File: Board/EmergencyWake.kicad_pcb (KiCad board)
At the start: 2 copper layers, 100 x 67 mm, 147 parts, among them J1 USB_C_Receptacle_USB2.0, J10 Conn_01x04, J2 Micro_SD_Card_Det, J3 Conn_01x03, J4 Conn_01x02, J5 Conn_01x05, J6 Conn_01x04, J7 Conn_01x02, J8 Conn_01x04, J9 Conn_01x04, Q1 AO3400A, Q2 AO3401A, Q3 AO3400A, SW1 SW_DPDT_x2, SW2 SW_Push, SW3 SW_Push, SW4 SW_Push, U1 M24C02-WMN, U10 L9110S, U11 SRV05-4, U2 AMS1117-3.3, U3 MC34063AD, U4 STM32F407VETx, U5 LM4670, U6 173950378, U7 PT6312B, U8 EL357N-G, U9 EL357N-G, Y1 32,768

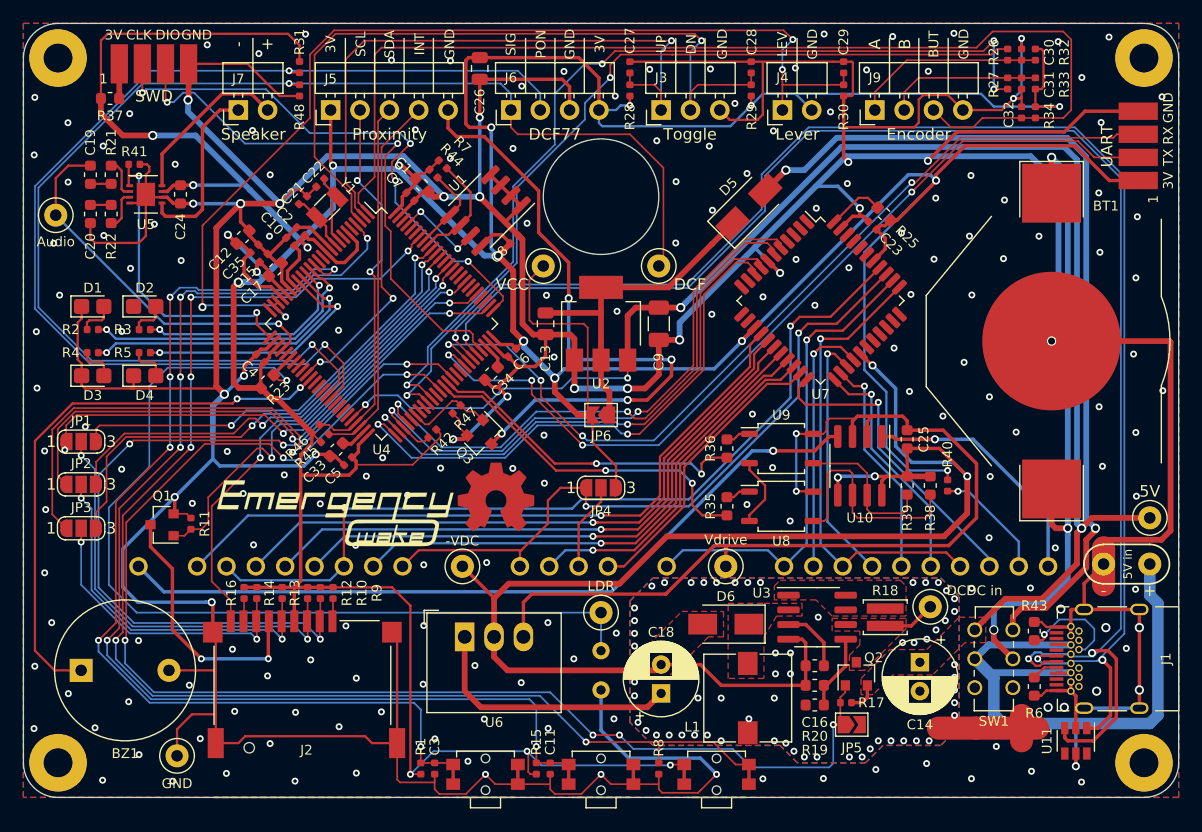
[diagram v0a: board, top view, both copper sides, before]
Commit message: [Board] Added OR gate for wakeup signal
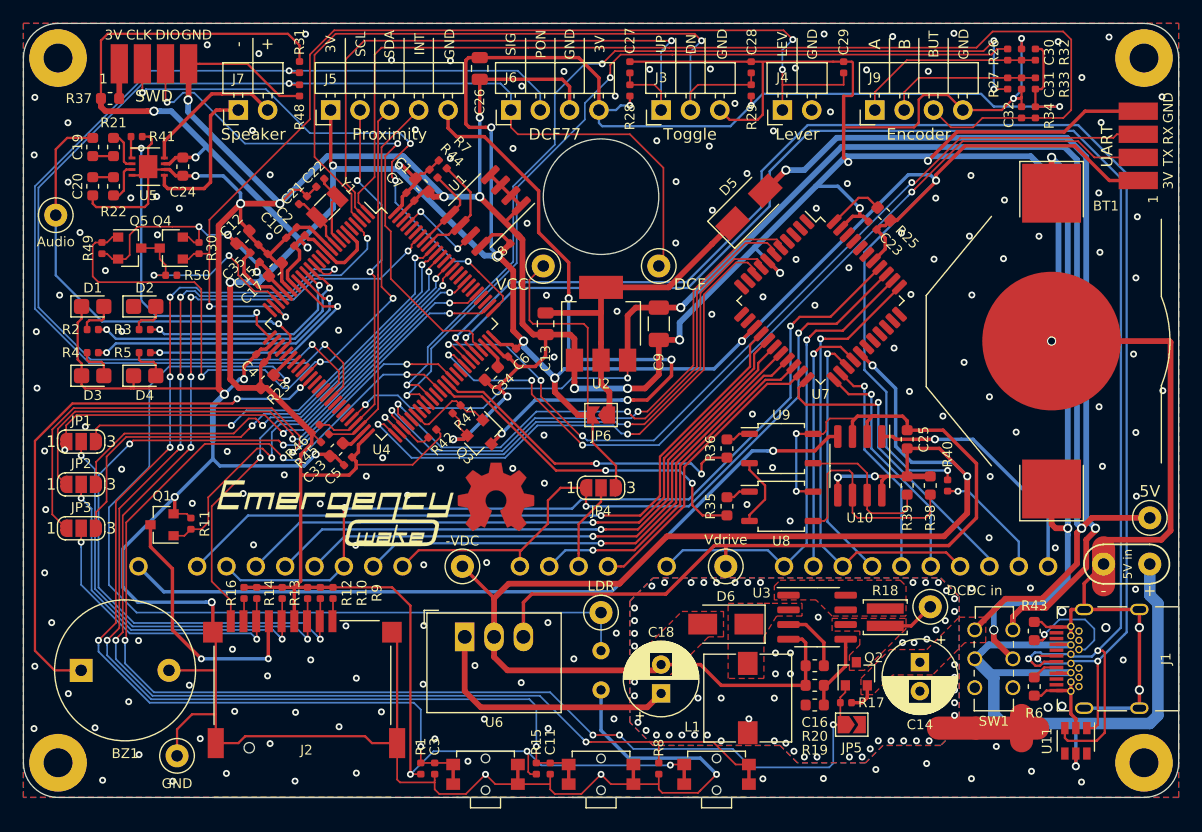
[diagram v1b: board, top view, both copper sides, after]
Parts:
- added Q4: AO3401A, Package_TO_SOT_SMD:SOT-23, F.Cu at (112.8, 119.5)
- added Q5: AO3401A, Package_TO_SOT_SMD:SOT-23, F.Cu at (109.2, 119.5)
- added R49: 100k, Resistor_SMD:R_0402_1005Metric, F.Cu at (106.8, 119.4)
- added R50: 100k, Resistor_SMD:R_0402_1005Metric, F.Cu at (112.8, 121.8)
- moved R30 57.4 mm to (115.2, 119.4), turned to 90 degrees
- moved C20 2.41 mm to (106.0, 114.1)
- moved R22 2.41 mm to (107.8, 114.1)
- moved R41 2.41 mm to (109.8, 109.8)
- moved U5 2.41 mm to (110.8, 112.4)
- moved C19 2.41 mm to (106.0, 110.7)
- moved C24 2.41 mm to (113.8, 112.4)
- moved R21 2.41 mm to (107.8, 110.7)
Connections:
- J4 pad 2: VCC -> GND
- R30 pad 2: GND -> VCC
- U4 pad 23: /LEVER -> /WAKEUP
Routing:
- net /I2C_INT: track 28.3 -> 63.0 mm, vias 2 -> 3
- net /WAKEUP: track 0.00 -> 18.8 mm, vias 0 -> 2
- net VCC: track 501.3 -> 512.9 mm, vias 21 -> 22
- net /AUDIO_OUT: track 32.8 -> 38.5 mm
- net /AUDIO_EN: track 26.5 -> 29.2 mm
- net /USB_DP: track 135.1 -> 132.8 mm
- net /SP+: track 15.5 -> 13.6 mm
- net /SP-: track 14.6 -> 12.7 mm
- net /USB_DM: track 129.9 -> 128.7 mm
- net /LEVER: track 91.1 -> 92.1 mm
- net GND: track 614.4 -> 614.5 mm, vias 202 -> 199

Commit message: [Board] New fabrication files
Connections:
- TP4 pad 1: VCC -> Net-(C13-Pad1)
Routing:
- net VCC: track 512.9 -> 495.1 mm
- net Net-(C13-Pad1): track 29.9 -> 34.0 mm
- net GND: vias 199 -> 209

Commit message: [Board] Some minor changes
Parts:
- removed the G*** at (149.0, 132.0)
- added C36: 22u,25V, Capacitor_SMD:C_0805_2012Metric, F.Cu at (123.0, 144.7)
- added G***: LOGO, Logo:EmergencyWake_Logo_20mm, B.Cu at (166.9, 154.0)
- C21, C22: value 6p -> 15p
- C26: value 10u,50V -> 10u,25V
- C9: value 10u,50V -> 10u,25V; footprint Capacitor_SMD:C_1206_3216Metric -> Capacitor_SMD:C_0805_2012Metric
- moved R11 0.10 mm to (114.5, 143.4)
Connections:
- C24 pad 1: VCC -> +5V
- U5 pad 7: VCC -> +5V
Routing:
- net +5V: track 132.6 -> 196.5 mm, vias 4 -> 7
- net GND: track 614.5 -> 577.2 mm, vias 209 -> 213
- net VCC: track 495.1 -> 490.3 mm, vias 22 -> 21
- net /SD_EN: track 37.3 -> 41.6 mm
- net /SD_DET: track 41.3 -> 39.9 mm
- net /SD_MOSI: track 38.4 -> 39.2 mm
- net Net-(DISP1-Pad32): track 67.0 -> 67.7 mm
- net /SWCLK: track 47.9 -> 48.6 mm
- net /SWDIO: track 48.6 -> 49.3 mm
- net Net-(J5-Pad5): track 55.2 -> 55.8 mm
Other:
- board text added: "BOOT0"
- board text added: "JH 2020"
- board text added: "Reset"
- board text added: "User"

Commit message: [Board] Final changes for order
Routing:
- net GND: track 577.2 -> 578.0 mm
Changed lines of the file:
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@@
   )
   (setup
-    (last_trace_width 0.5)
+    (last_trace_width 0.15)
     (user_trace_width 0.15)
     (user_trace_width 0.2)
@@
   (segment (start 187.2 111.5) (end 178.7 111.5) (width 0.5) (layer B.Cu) (net 4))
   (segment (start 178.7 111.5) (end 171.2 111.5) (width 0.5) (layer B.Cu) (net 4))
-  (segment (start 178.7 111.5) (end 178.686812 111.5) (width 0.3) (layer B.Cu) (net 4))
-  (segment (start 178.643405 111.543407) (end 178.293406 111.893406) (width 0.3) (layer B.Cu) (net 4))
-  (via (at 178.293406 111.893406) (size 0.7) (drill 0.4) (layers F.Cu B.Cu) (net 4))
-  (segment (start 178.686812 111.5) (end 178.643405 111.543407) (width 0.3) (layer B.Cu) (net 4))
   (segment (start 168.6 114.1) (end 170.5 114.1) (width 0.3) (layer B.Cu) (net 4))
   (segment (start 171.2 111.5) (end 168.6 114.1) (width 0.5) (layer B.Cu) (net 4))
@@
   (segment (start 142.842947 118.357053) (end 139.5 115.014106) (width 0.5) (layer F.Cu) (net 4))
   (via (at 139.5 115.000016) (size 0.8) (drill 0.5) (layers F.Cu B.Cu) (net 4))
-  (segment (start 178.3 111.9) (end 178.293406 111.893406) (width 0.3) (layer F.Cu) (net 4))
-  (segment (start 196.5 107.6) (end 191.9 107.6) (width 0.3) (layer F.Cu) (net 4))
-  (segment (start 180.8 109.4) (end 178.3 111.9) (width 0.3) (layer F.Cu) (net 4))
-  (segment (start 191.9 107.6) (end 190.1 109.4) (width 0.3) (layer F.Cu) (net 4))
-  (segment (start 190.1 109.4) (end 180.8 109.4) (width 0.3) (layer F.Cu) (net 4))
   (segment (start 116.4 133.1) (end 116.4 136.1) (width 0.5) (layer B.Cu) (net 4))
   (segment (start 117.4 132.1) (end 116.4 133.1) (width 0.5) (layer B.Cu) (net 4))
@@
   (via (at 163.105521 133.817651) (size 0.6) (drill 0.3) (layers F.Cu B.Cu) (net 4))
   (via (at 164.019613 123.671872) (size 0.6) (drill 0.3) (layers F.Cu B.Cu) (net 4))
-  (via (at 165.1 163.9) (size 0.6) (drill 0.3) (layers F.Cu B.Cu) (net 4))
+  (via (at 165.1 163.3) (size 0.6) (drill 0.3) (layers F.Cu B.Cu) (net 4))
   (via (at 164.922726 109.308582) (size 0.6) (drill 0.3) (layers F.Cu B.Cu) (net 4))
   (via (at 164.849931 138.452065) (size 0.6) (drill 0.3) (layers F.Cu B.Cu) (net 4))
@@
   (segment (start 158.600001 163.900001) (end 158.9 164.2) (width 0.3) (layer B.Cu) (net 4))
   (segment (start 150 157.7) (end 150 161.2) (width 0.3) (layer B.Cu) (net 4))
+  (via (at 177.8 111.599994) (size 0.7) (drill 0.4) (layers F.Cu B.Cu) (net 4))
+  (segment (start 178.294974 111.599994) (end 177.8 111.599994) (width 0.3) (layer B.Cu) (net 4))
+  (segment (start 179.999994 109.4) (end 178.149999 111.249995) (width 0.3) (layer F.Cu) (net 4))
+  (segment (start 178.7 111.5) (end 178.600006 111.599994) (width 0.3) (layer B.Cu) (net 4))
+  (segment (start 178.600006 111.599994) (end 178.294974 111.599994) (width 0.3) (layer B.Cu) (net 4))
+  (segment (start 178.149999 111.249995) (end 177.8 111.599994) (width 0.3) (layer F.Cu) (net 4))
+  (segment (start 191.9 107.6) (end 190.1 109.4) (width 0.3) (layer F.Cu) (net 4))
+  (segment (start 190.1 109.4) (end 179.999994 109.4) (width 0.3) (layer F.Cu) (net 4))
+  (segment (start 196.5 107.6) (end 191.9 107.6) (width 0.3) (layer F.Cu) (net 4))
   (via (at 189 111.6) (size 0.8) (drill 0.5) (layers F.Cu B.Cu) (net 5))
   (segment (start 189 114.7) (end 189 111.6) (width 0.5) (layer F.Cu) (net 5))
@@
   (segment (start 118.870953 119.056847) (end 119.657053 119.842947) (width 0.3) (layer F.Cu) (net 7))
   (segment (start 118.443153 119.056847) (end 118.870953 119.056847) (width 0.3) (layer F.Cu) (net 7))
-  (segment (start 113.1875 111.6125) (end 113.8 111.6125) (width 0.3) (layer F.Cu) (net 53))
-  (segment (start 112.650001 112.149999) (end 113.1875 111.6125) (width 0.3) (layer F.Cu) (net 53))
-  (segment (start 112.2 112.149999) (end 112.650001 112.149999) (width 0.3) (layer F.Cu) (net 53))
   (segment (start 140.594077 118.3) (end 139.596949 119.297128) (width 0.3) (layer F.Cu) (net 7))
   (segment (start 141.414106 118.3) (end 140.594077 118.3) (width 0.3) (layer F.Cu) (net 7))
@@
   (segment (start 117.7 118.3) (end 117.7 118.313694) (width 0.3) (layer F.Cu) (net 7))
   (segment (start 124.957053 135.442947) (end 125.757053 136.242947) (width 0.15) (layer F.Cu) (net 7))
-  (segment (start 113.8125 111.6) (end 113.8 111.6125) (width 0.3) (layer F.Cu) (net 53))
   (segment (start 149.82 104.72) (end 149.82 107.5) (width 0.3) (layer F.Cu) (net 7))
   (segment (start 148.0625 102.9625) (end 149.82 104.72) (width 0.3) (layer F.Cu) (net 7))
@@
   (segment (start 136.780598 131.073491) (end 137.607107 131.9) (width 0.2) (layer F.Cu) (net 52))
   (segment (start 139.8 131.9) (end 146 138.1) (width 0.2) (layer F.Cu) (net 52))
+  (segment (start 113.1875 111.6125) (end 113.8 111.6125) (width 0.3) (layer F.Cu) (net 53))
+  (segment (start 112.650001 112.149999) (end 113.1875 111.6125) (width 0.3) (layer F.Cu) (net 53))
+  (segment (start 112.2 112.149999) (end 112.650001 112.149999) (width 0.3) (layer F.Cu) (net 53))
+  (segment (start 113.8125 111.6) (end 113.8 111.6125) (width 0.3) (layer F.Cu) (net 53))
   (segment (start 173.05 158.35) (end 173.05 157.3) (width 0.3) (layer F.Cu) (net 53))
   (segment (start 172.6 158.8) (end 173.05 158.35) (width 0.3) (layer F.Cu) (net 53))

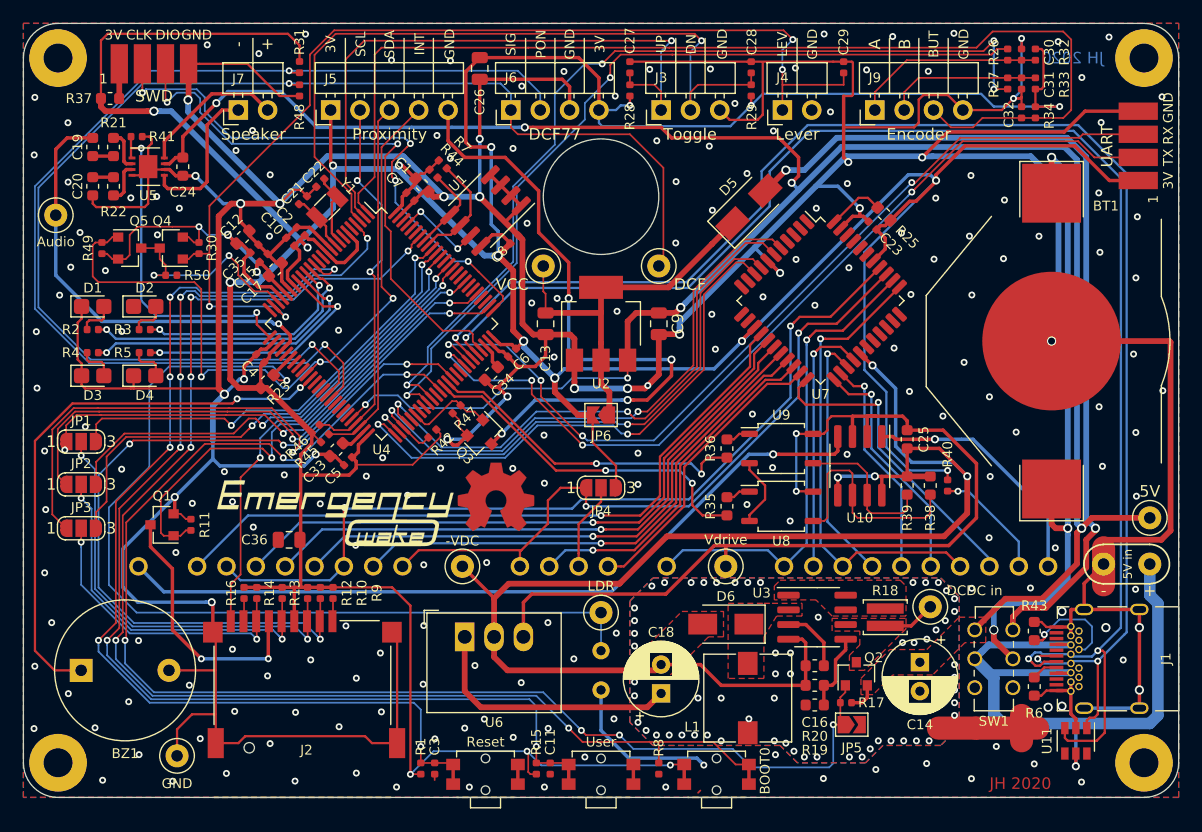
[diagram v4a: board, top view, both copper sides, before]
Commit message: [Board] Replaced audio amplifier
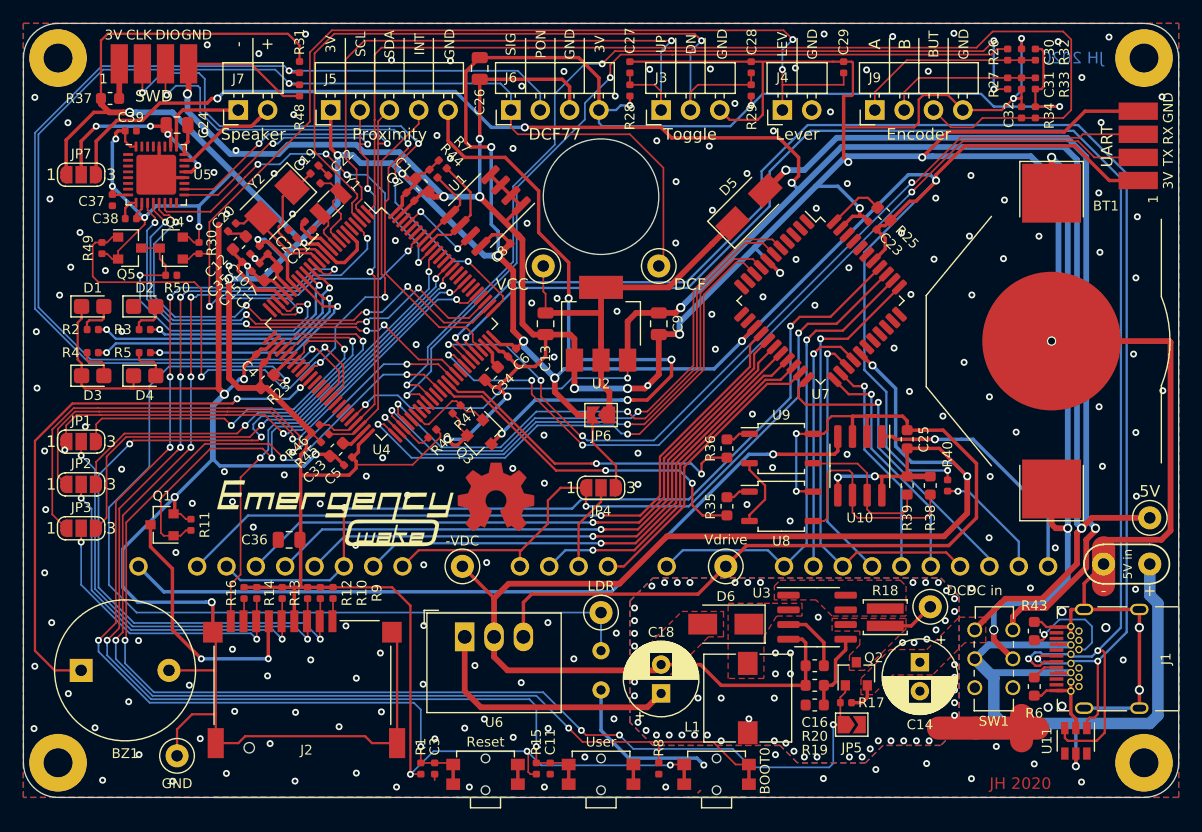
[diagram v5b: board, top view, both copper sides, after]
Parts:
- removed R21, R22: 300k, Resistor_SMD:R_0603_1608Metric
- removed R41: 100k, Resistor_SMD:R_0402_1005Metric
- removed TP7: Audio, TestPoint:TestPoint_Loop_D1.80mm_Drill1.0mm_Beaded
- added C37: 100n, Capacitor_SMD:C_0402_1005Metric, F.Cu at (107.7, 115.3)
- added C38: 100n, Capacitor_SMD:C_0402_1005Metric, F.Cu at (109.3, 116.9)
- added C39: 100n, Capacitor_SMD:C_0402_1005Metric, F.Cu at (109.3, 109.3)
- added JP7: SolderJumper_3_Open, Jumper:SolderJumper-3_P1.3mm_Open_RoundedPad1.0x1.5mm_NumberLabels, F.Cu at (105.0, 113.1)
- added Y2: 8M, Crystal:Crystal_SMD_5032-2Pin_5.0x3.2mm, F.Cu at (122.0, 115.5)
- C19, C20: value 10n -> 30p; footprint Capacitor_SMD:C_0603_1608Metric -> Capacitor_SMD:C_0402_1005Metric
- C24: value 1u,50V -> 10u,25V; footprint Capacitor_SMD:C_0603_1608Metric -> Capacitor_SMD:C_0805_2012Metric
- U5: value LM4670 -> WM8960; footprint Package_SON:WSON-8-1EP_3x3mm_P0.5mm_EP1.6x2.0mm -> Package_DFN_QFN:QFN-32-1EP_5x5mm_P0.5mm_EP3.45x3.45mm
- moved C19 19.3 mm to (125.2, 112.7), turned to 45 degrees
- moved C20 12.6 mm to (118.0, 117.7), turned to 225 degrees
- moved C24 3.63 mm to (113.3, 108.8), turned to 0 degrees
- moved C10 2.40 mm to (120.8, 119.6), turned to 315 degrees
- moved C21 2.26 mm to (124.7, 117.5), turned to 135 degrees
- moved C15 1.06 mm to (120.1, 121.1)
- moved C35 1.06 mm to (119.3, 120.3)
- moved U5 0.99 mm to (111.5, 113.1)
- moved C2 0.73 mm to (123.3, 118.2)
- moved C12 0.58 mm to (118.7, 119.0)
- moved C17 0.57 mm to (121.4, 121.7)
- moved C22 0.46 mm to (126.0, 113.5), turned to 45 degrees
- moved Y1 0.42 mm to (126.6, 115.6)
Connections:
- net Net-(U4-Pad79) renamed /I2S_extSD
- C19 pad 2: /AUDIO_OUT -> GND
- C20 pad 1: GND -> Net-(C20-Pad1)
- C20 pad 2: Net-(C20-Pad2) -> GND
- C24 pad 1: +5V -> Net-(C24-Pad1)
- J7 pad 1: /SP+ -> /SPK_LP
- J7 pad 2: /SP- -> /SPK_LN
- U4 pad 12: Net-(U4-Pad12) -> Net-(C19-Pad1)
- U4 pad 13: Net-(U4-Pad13) -> Net-(C20-Pad1)
- U4 pad 26: /AUDIO_EN -> Net-(U4-Pad26)
- U4 pad 29: /AUDIO_OUT -> /SD_CS
- U4 pad 30: Net-(U4-Pad30) -> /SD_SCK
- U4 pad 32: Net-(U4-Pad32) -> /SD_MOSI
- U4 pad 66: Net-(U4-Pad66) -> /MCLK
- U4 pad 77: /SD_CS -> /I2S_WS
- U4 pad 78: Net-(U4-Pad78) -> /I2S_CK
- U4 pad 89: /SD_SCK -> Net-(U4-Pad89)
- U4 pad 91: /SD_MOSI -> /I2S_SD
- U5 pad 1: /AUDIO_EN -> Net-(U5-Pad1)
- U5 pad 4: GND -> Net-(U5-Pad4)
- U5 pad 5: /SP+ -> Net-(U5-Pad5)
- U5 pad 6: GND -> Net-(U5-Pad6)
- U5 pad 7: +5V -> Net-(U5-Pad7)
- U5 pad 8: /SP- -> VCC
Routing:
- net /I2S_WS: track 0.00 -> 43.5 mm, vias 0 -> 4
- net /I2S_CK: track 0.00 -> 42.4 mm, vias 0 -> 4
- net /MCLK: track 0.00 -> 38.8 mm, vias 0 -> 4
- net /AUDIO_OUT: track 38.5 -> 0.00 mm, vias 1 -> 0
- net /I2S_SD: track 0.00 -> 32.1 mm, vias 0 -> 4
- net GND: track 578.0 -> 547.4 mm, vias 213 -> 212
- net /AUDIO_EN: track 29.2 -> 0.00 mm, vias 2 -> 0
- net VCC: track 490.3 -> 514.9 mm, vias 21 -> 24
- net /I2C_SDA: track 31.4 -> 52.1 mm, vias 0 -> 2
- net Net-(C24-Pad1): track 0.00 -> 18.9 mm, vias 0 -> 4
- net /I2C_SCL: track 32.9 -> 51.0 mm, vias 2 -> 4
- net /SP+: track 13.1 -> 0.00 mm
- net /SP-: track 12.7 -> 0.00 mm
- net /WAKEUP: track 18.8 -> 28.9 mm
- net Net-(C19-Pad1): track 1.80 -> 11.2 mm
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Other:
- board text removed: "Audio"
